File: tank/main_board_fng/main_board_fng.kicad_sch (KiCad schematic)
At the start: 46 parts, among them J11 M0, J12 M1, J13 M2, U1 L7805, U2 ATMEGA328P-PU, U3 SN74HC595, U4 TB6612FNG, U5 TB6612FNG, Y1 Crystal

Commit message: FNG WIP
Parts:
- removed J12: M1, Connector_JST:JST_EH_B2B-EH-A_1x02_P2.50mm_Vertical, symbol custom:Conn_01x02_Male
- added J1: M1, Connector_JST:JST_EH_B2B-EH-A_1x02_P2.50mm_Vertical, symbol custom:Conn_01x02_Male
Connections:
- net 4.5V: now also C11.2, C9.2, U5.19 (STBY), U5.20 (VCC)
- net Vm: now also C12.2, C13.2, U5.13 (VM2), U5.14 (VM3), U5.24 (VM1)
- net at U4.7 (BO2), U4.8 (BO2): now also J1.2 (Pin_2)
- net at U4.11 (BO1), U4.12 (BO1): now also J1.1 (Pin_1)
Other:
- moved on the sheet: J11, J13

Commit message: main board v0.14
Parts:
- J1, J11, J13, PowerMotor1: footprint Connector_JST:JST_EH_B2B-EH-A_1x02_P2.50mm_Vertical -> TerminalBlock_Phoenix:TerminalBlock_Phoenix_MKDS-1,5-2_1x02_P5.00mm_Horizontal
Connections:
- net at U4.5 (AO2), U4.6 (AO2): now also J11.2 (Pin_2); no longer J11.1 (Pin_1)
- net at U4.1 (AO1), U4.2 (AO1): now also J11.1 (Pin_1); no longer J11.2 (Pin_2)
- net at U5.5 (AO2), U5.6 (AO2): now also J13.2 (Pin_2); no longer J13.1 (Pin_1)
- net at U5.1 (AO1), U5.2 (AO1): now also J13.1 (Pin_1); no longer J13.2 (Pin_2)
- net at U4.11 (BO1), U4.12 (BO1): now also J1.2 (Pin_2); no longer J1.1 (Pin_1)
- net at U4.7 (BO2), U4.8 (BO2): now also J1.1 (Pin_1); no longer J1.2 (Pin_2)
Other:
- moved on the sheet: J13
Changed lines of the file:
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@@
 	(wire
 		(pts
-			(xy 213.36 64.77) (xy 210.82 64.77)
-		)
-		(stroke
-			(width 0)
-			(type default)
-		)
-	)
-	(wire
-		(pts
-			(xy 210.82 74.93) (xy 209.55 74.93)
+			(xy 36.83 110.49) (xy 74.93 110.49)
 		)
 		(stroke
@@
 	(wire
 		(pts
-			(xy 36.83 110.49) (xy 74.93 110.49)
+			(xy 210.82 71.12) (xy 212.09 71.12)
 		)
 		(stroke
@@
 	(wire
 		(pts
-			(xy 210.82 74.93) (xy 210.82 76.2)
-		)
-		(stroke
-			(width 0)
-			(type default)
-		)
-	)
-	(wire
-		(pts
 			(xy 140.97 67.31) (xy 137.16 67.31)
 		)
@@
 	(wire
 		(pts
-			(xy 213.36 58.42) (xy 213.36 59.69)
-		)
-		(stroke
-			(width 0)
-			(type default)
-		)
-	)
-	(wire
-		(pts
 			(xy 153.67 46.99) (xy 152.4 46.99)
 		)
@@
 	(wire
 		(pts
-			(xy 212.09 72.39) (xy 212.09 74.93)
+			(xy 210.82 124.46) (xy 214.63 124.46)
 		)
 		(stroke
@@
 	(wire
 		(pts
-			(xy 213.36 73.66) (xy 213.36 72.39)
+			(xy 137.16 67.31) (xy 137.16 63.5)
 		)
 		(stroke
@@
 	(wire
 		(pts
-			(xy 137.16 67.31) (xy 137.16 63.5)
+			(xy 210.82 74.93) (xy 213.36 74.93)
 		)
 		(stroke
@@
 	(wire
 		(pts
-			(xy 59.69 26.67) (xy 59.69 74.93)
+			(xy 212.09 125.73) (xy 217.17 125.73)
 		)
 		(stroke
@@
 	(wire
 		(pts
-			(xy 210.82 130.81) (xy 210.82 129.54)
+			(xy 210.82 129.54) (xy 212.09 129.54)
+		)
+		(stroke
+			(width 0)
+			(type default)
+		)
+	)
+	(wire
+		(pts
+			(xy 59.69 26.67) (xy 59.69 74.93)
 		)
 		(stroke
@@
 	(wire
 		(pts
+			(xy 212.09 58.42) (xy 212.09 62.23)
+		)
+		(stroke
+			(width 0)
+			(type default)
+		)
+	)
+	(wire
+		(pts
 			(xy 123.19 69.85) (xy 123.19 77.47)
 		)
@@
 	(wire
 		(pts
-			(xy 200.66 40.64) (xy 200.66 43.18)
+			(xy 210.82 76.2) (xy 210.82 74.93)
 		)
 		(stroke
@@
 	(wire
 		(pts
-			(xy 55.88 26.67) (xy 59.69 26.67)
+			(xy 200.66 40.64) (xy 200.66 43.18)
 		)
 		(stroke
@@
 	(wire
 		(pts
-			(xy 132.08 49.53) (xy 140.97 49.53)
+			(xy 55.88 26.67) (xy 59.69 26.67)
 		)
 		(stroke
@@
 	(wire
 		(pts
-			(xy 214.63 124.46) (xy 210.82 124.46)
+			(xy 132.08 49.53) (xy 140.97 49.53)
 		)
 		(stroke
@@
 	(wire
 		(pts
-			(xy 209.55 74.93) (xy 209.55 73.66)
-		)
-		(stroke
-			(width 0)
-			(type default)
-		)
-	)
-	(wire
-		(pts
-			(xy 214.63 124.46) (xy 214.63 125.73)
+			(xy 214.63 124.46) (xy 214.63 128.27)
 		)
 		(stroke
@@
 	(wire
 		(pts
-			(xy 213.36 58.42) (xy 210.82 58.42)
-		)
-		(stroke
-			(width 0)
-			(type default)
-		)
-	)
-	(wire
-		(pts
 			(xy 102.87 110.49) (xy 120.015 110.49)
 		)
@@
 	(wire
 		(pts
-			(xy 41.91 125.73) (xy 48.895 125.73)
+			(xy 210.82 58.42) (xy 212.09 58.42)
 		)
 		(stroke
@@
 	(wire
 		(pts
-			(xy 214.63 130.81) (xy 210.82 130.81)
+			(xy 41.91 125.73) (xy 48.895 125.73)
 		)
 		(stroke
@@
 	(wire
 		(pts
-			(xy 210.82 64.77) (xy 210.82 63.5)
+			(xy 212.09 72.39) (xy 213.36 72.39)
 		)
 		(stroke
@@
 	(wire
 		(pts
-			(xy 210.82 71.12) (xy 210.82 72.39)
+			(xy 184.15 120.65) (xy 180.34 120.65)
 		)
 		(stroke
@@
 	(wire
 		(pts
-			(xy 184.15 120.65) (xy 180.34 120.65)
+			(xy 102.87 110.49) (xy 102.87 123.19)
 		)
 		(stroke
@@
 	(wire
 		(pts
-			(xy 102.87 110.49) (xy 102.87 123.19)
+			(xy 41.91 91.44) (xy 41.91 103.505)
 		)
 		(stroke
@@
 	(wire
 		(pts
-			(xy 41.91 91.44) (xy 41.91 103.505)
+			(xy 48.895 125.73) (xy 48.895 130.81)
 		)
 		(stroke
@@
 	(wire
 		(pts
-			(xy 48.895 125.73) (xy 48.895 130.81)
+			(xy 198.12 93.98) (xy 203.2 93.98)
 		)
 		(stroke
@@
 	(wire
 		(pts
-			(xy 198.12 93.98) (xy 203.2 93.98)
+			(xy 110.49 69.85) (xy 123.19 69.85)
 		)
 		(stroke
@@
 	(wire
 		(pts
-			(xy 110.49 69.85) (xy 123.19 69.85)
+			(xy 110.49 44.45) (xy 137.16 44.45)
 		)
 		(stroke
@@
 	(wire
 		(pts
-			(xy 210.82 72.39) (xy 212.09 72.39)
+			(xy 143.51 72.39) (xy 143.51 91.44)
 		)
 		(stroke
@@
 	(wire
 		(pts
-			(xy 110.49 44.45) (xy 137.16 44.45)
+			(xy 200.66 109.22) (xy 203.2 109.22)
 		)
 		(stroke
@@
 	(wire
 		(pts
-			(xy 143.51 72.39) (xy 143.51 91.44)
+			(xy 127 60.96) (xy 147.32 60.96)
 		)
 		(stroke
@@
 	(wire
 		(pts
-			(xy 200.66 109.22) (xy 203.2 109.22)
+			(xy 210.82 59.69) (xy 213.36 59.69)
 		)
 		(stroke
@@
 	(wire
 		(pts
-			(xy 127 60.96) (xy 147.32 60.96)
+			(xy 203.2 43.18) (xy 210.82 43.18)
 		)
 		(stroke
@@
 	(wire
 		(pts
-			(xy 212.09 74.93) (xy 213.36 74.93)
+			(xy 184.15 109.22) (xy 187.96 109.22)
 		)
 		(stroke
@@
 	(wire
 		(pts
-			(xy 203.2 43.18) (xy 210.82 43.18)
+			(xy 214.63 128.27) (xy 217.17 128.27)
 		)
 		(stroke
@@
 	(wire
 		(pts
-			(xy 184.15 109.22) (xy 187.96 109.22)
+			(xy 212.09 62.23) (xy 213.36 62.23)
 		)
 		(stroke
@@
 	(wire
 		(pts
+			(xy 210.82 63.5) (xy 210.82 59.69)
+		)
+		(stroke
+			(width 0)
+			(type default)
+		)
+	)
+	(wire
+		(pts
 			(xy 74.93 138.43) (xy 79.375 138.43)
 		)
@@
 	(wire
 		(pts
-			(xy 209.55 73.66) (xy 213.36 73.66)
+			(xy 200.66 43.18) (xy 203.2 43.18)
 		)
 		(stroke
@@
 	(wire
 		(pts
-			(xy 200.66 43.18) (xy 203.2 43.18)
+			(xy 140.97 67.31) (xy 143.51 67.31)
 		)
 		(stroke
@@
 	(wire
 		(pts
-			(xy 140.97 67.31) (xy 143.51 67.31)
+			(xy 215.9 109.22) (xy 224.79 109.22)
 		)
 		(stroke
@@
 	(wire
 		(pts
-			(xy 215.9 109.22) (xy 224.79 109.22)
+			(xy 212.09 71.12) (xy 212.09 72.39)
 		)
 		(stroke
@@
 	(wire
 		(pts
-			(xy 214.63 128.27) (xy 214.63 130.81)
-		)
-		(stroke
-			(width 0)
-			(type default)
-		)
-	)
-	(wire
-		(pts
 			(xy 120.015 130.175) (xy 120.015 133.35)
 		)
@@
 	(wire
 		(pts
-			(xy 62.23 153.67) (xy 62.23 143.51)
+			(xy 212.09 129.54) (xy 212.09 125.73)
 		)
 		(stroke
@@
 	(wire
 		(pts
-			(xy 213.36 62.23) (xy 213.36 64.77)
+			(xy 62.23 153.67) (xy 62.23 143.51)
 		)
 		(stroke
@@
 			)
 		)
-		(property "Footprint" "Connector_JST:JST_EH_B2B-EH-A_1x02_P2.50mm_Vertical"
+		(property "Footprint" "TerminalBlock_Phoenix:TerminalBlock_Phoenix_MKDS-1,5-2_1x02_P5.00mm_Horizontal"
 			(at 36.195 147.32 0)
 			(effects
@@
 			)
 		)
-		(property "Footprint" "Connector_JST:JST_EH_B2B-EH-A_1x02_P2.50mm_Vertical"
+		(property "Footprint" "TerminalBlock_Phoenix:TerminalBlock_Phoenix_MKDS-1,5-2_1x02_P5.00mm_Horizontal"
 			(at 218.44 62.23 0)
 			(effects
@@
 	(symbol
 		(lib_id "custom:Conn_01x02_Male")
-		(at 219.71 128.27 180)
+		(at 222.25 128.27 180)
 		(unit 1)
 		(exclude_from_sim no)
@@
 		(dnp no)
 		(property "Reference" "J13"
-			(at 219.71 130.81 0)
+			(at 222.25 130.81 0)
 			(effects
 				(font
@@
 		)
 		(property "Value" "M2"
-			(at 219.71 123.19 0)
+			(at 222.25 123.19 0)
 			(effects
 				(font
@@
 			)
 		)
-		(property "Footprint" "Connector_JST:JST_EH_B2B-EH-A_1x02_P2.50mm_Vertical"
-			(at 219.71 128.27 0)
+		(property "Footprint" "TerminalBlock_Phoenix:TerminalBlock_Phoenix_MKDS-1,5-2_1x02_P5.00mm_Horizontal"
+			(at 222.25 128.27 0)
 			(effects
 				(font
@@
 		)
 		(property "Datasheet" ""
-			(at 219.71 128.27 0)
+			(at 222.25 128.27 0)
 			(effects
 				(font
@@
 		)
 		(property "Description" ""
-			(at 219.71 128.27 0)
+			(at 222.25 128.27 0)
 			(effects
 				(font
@@
 			)
 		)
-		(property "Footprint" "Connector_JST:JST_EH_B2B-EH-A_1x02_P2.50mm_Vertical"
+		(property "Footprint" "TerminalBlock_Phoenix:TerminalBlock_Phoenix_MKDS-1,5-2_1x02_P5.00mm_Horizontal"
 			(at 218.44 74.93 0)
 			(effects

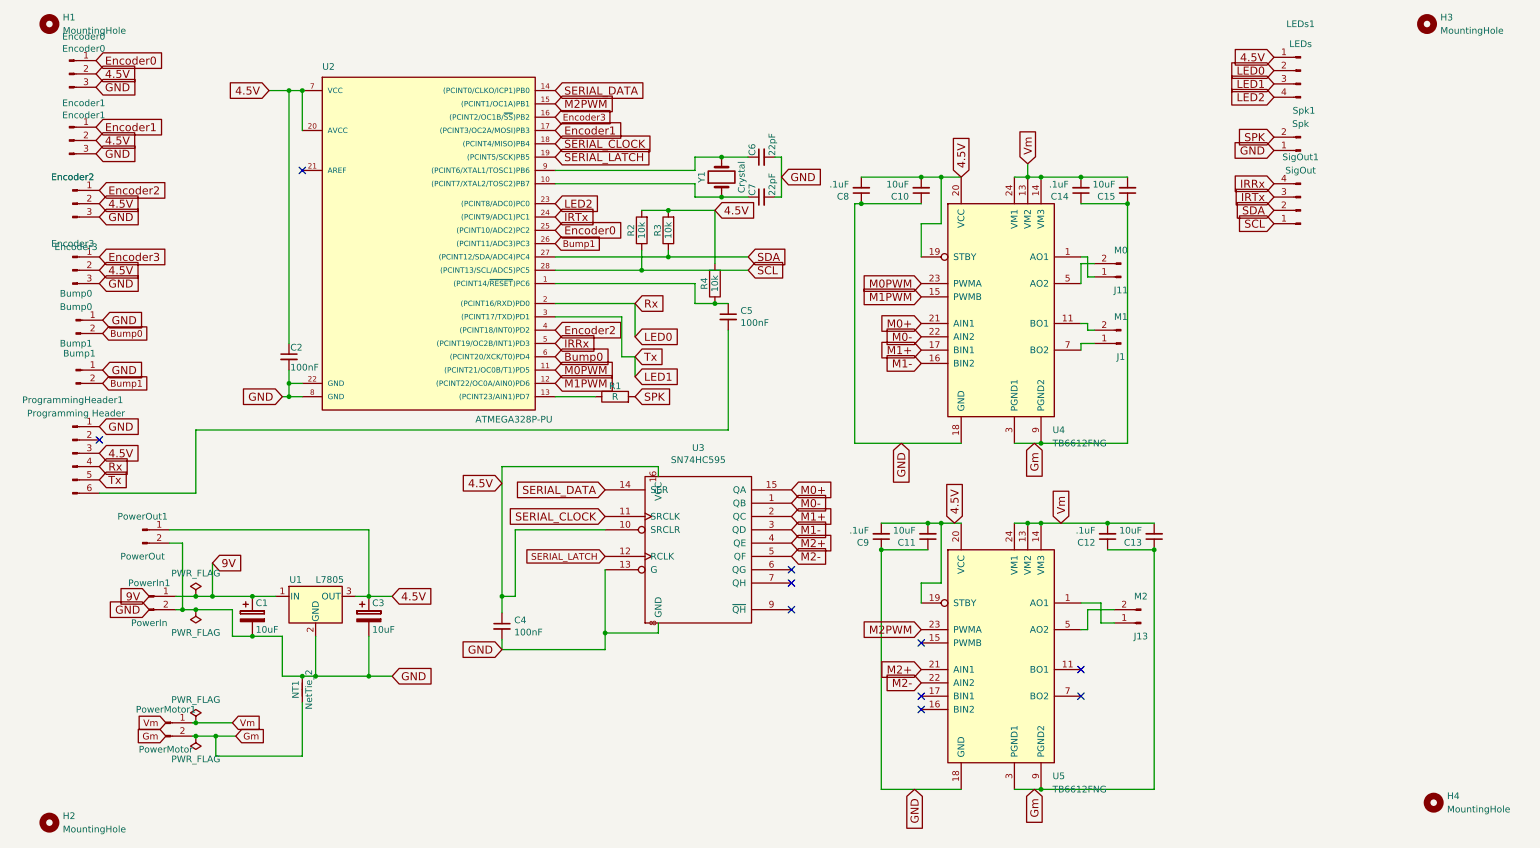
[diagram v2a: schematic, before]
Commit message: Main Board v0.15
Changes:
    - back to L293 motor driver
    - add speaker resistor
    - 3.5mm pitch screw terminals for motors and motor power
    - move programming header
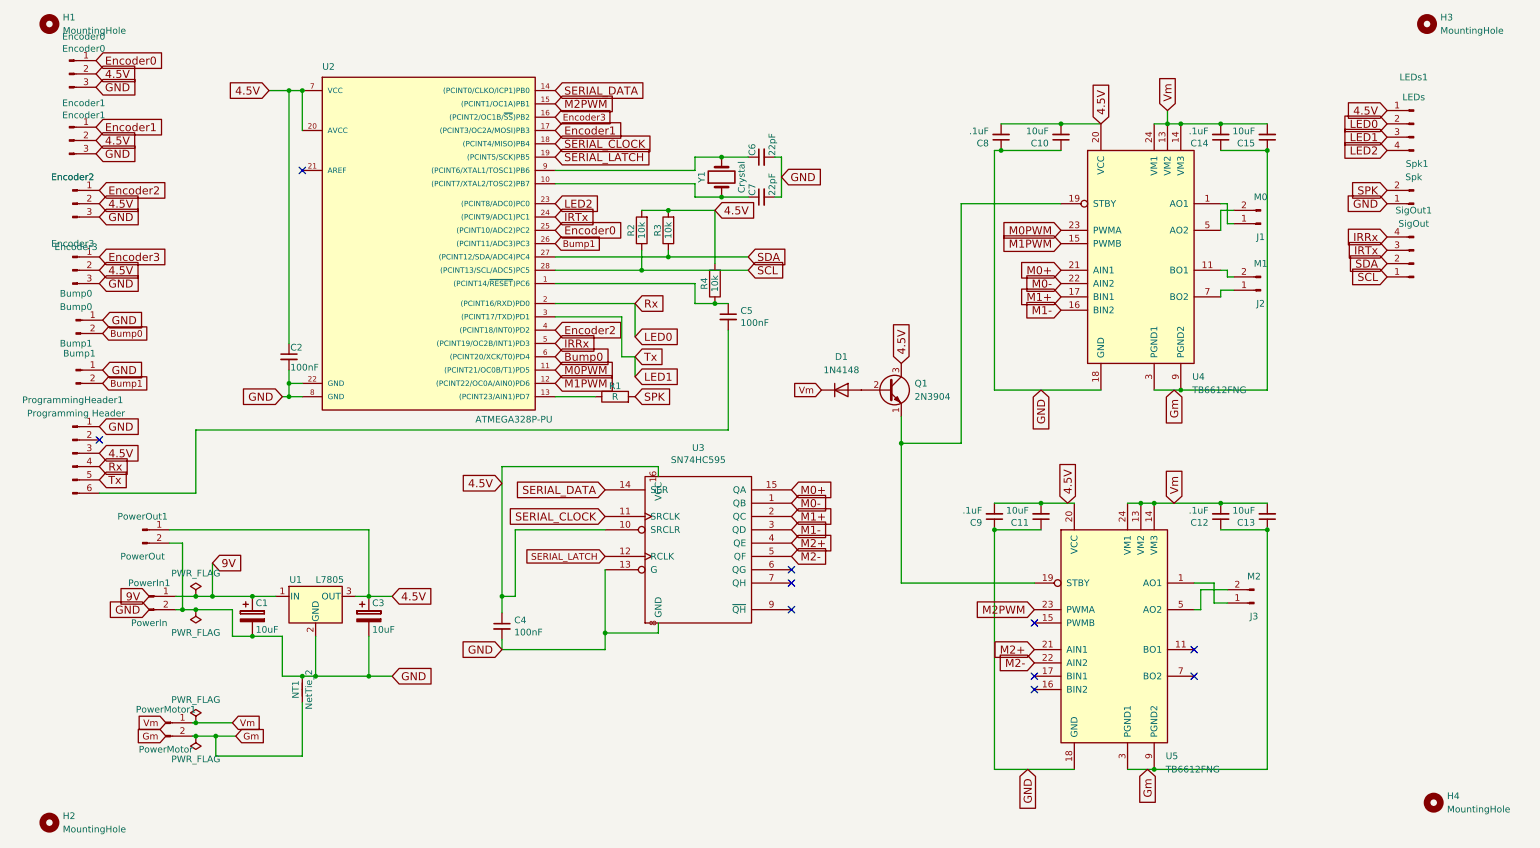
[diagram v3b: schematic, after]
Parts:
- removed J11: M0, TerminalBlock_Phoenix:TerminalBlock_Phoenix_MKDS-1,5-2_1x02_P5.00mm_Horizontal, symbol custom:Conn_01x02_Male
- removed J13: M2, TerminalBlock_Phoenix:TerminalBlock_Phoenix_MKDS-1,5-2_1x02_P5.00mm_Horizontal, symbol custom:Conn_01x02_Male
- added D1: 1N4148, Diode_THT:D_DO-15_P5.08mm_Vertical_AnodeUp, symbol Diode:1N4148
- added J2: M1, TerminalBlock_Phoenix:TerminalBlock_Phoenix_PT-1,5-2-3.5-H_1x02_P3.50mm_Horizontal, symbol custom:Conn_01x02_Male
- added J3: M2, TerminalBlock_Phoenix:TerminalBlock_Phoenix_PT-1,5-2-3.5-H_1x02_P3.50mm_Horizontal, symbol custom:Conn_01x02_Male
- added Q1: 2N3904, Package_TO_SOT_THT:TO-92_Inline, symbol Transistor_BJT:2N3904
- J1: value M1 -> M0; footprint TerminalBlock_Phoenix:TerminalBlock_Phoenix_MKDS-1,5-2_1x02_P5.00mm_Horizontal -> TerminalBlock_Phoenix:TerminalBlock_Phoenix_PT-1,5-2-3.5-H_1x02_P3.50mm_Horizontal
- PowerMotor1: footprint TerminalBlock_Phoenix:TerminalBlock_Phoenix_MKDS-1,5-2_1x02_P5.00mm_Horizontal -> TerminalBlock_Phoenix:TerminalBlock_Phoenix_PT-1,5-2-3.5-H_1x02_P3.50mm_Horizontal
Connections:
- net 4.5V: now also Q1.3 (C); no longer U4.19 (STBY), U5.19 (STBY)
- net Vm: now also D1.1 (K)
- net at U4.1 (AO1), U4.2 (AO1): now also J1.1 (Pin_1)
- net at U4.5 (AO2), U4.6 (AO2): now also J1.2 (Pin_2)
- net at U5.1 (AO1), U5.2 (AO1): now also J3.1 (Pin_1)
- net at U5.5 (AO2), U5.6 (AO2): now also J3.2 (Pin_2)
- net at U4.7 (BO2), U4.8 (BO2): now also J2.1 (Pin_1); no longer J1.1 (Pin_1)
- net at U4.11 (BO1), U4.12 (BO1): now also J2.2 (Pin_2); no longer J1.2 (Pin_2)
- new net: D1.2 (A), Q1.2 (B)
- new net: Q1.1 (E), U4.19 (STBY), U5.19 (STBY)
